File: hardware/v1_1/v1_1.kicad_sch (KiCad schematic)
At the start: 74 parts, among them J1 AUDIO IN, J2 MIDI OUT, J3 MIDI IN, J4 MIDI THRU, J5 OUTPUT R, J6 OUTPUT L - MONO, J7 EXP 2, J8 EXP 1, J9 Batt In, SW1 RotaryEncoder_Switch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

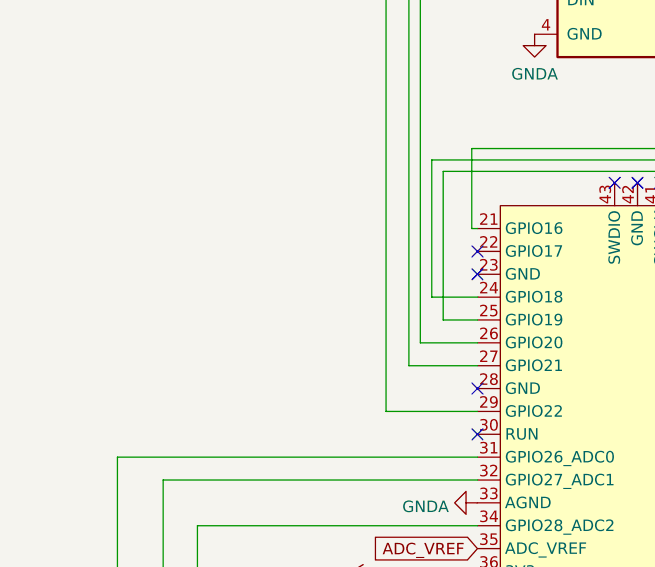
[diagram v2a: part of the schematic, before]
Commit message: Added low battery sensing on digitalPin
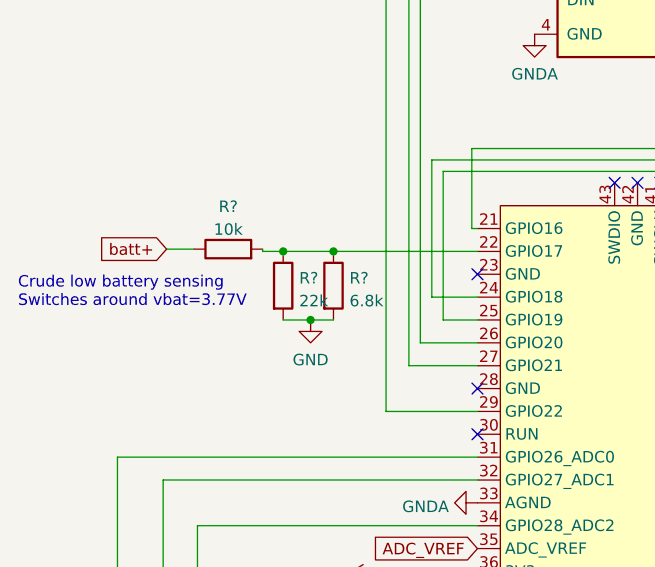
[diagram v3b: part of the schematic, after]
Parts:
- added R?: 10k, symbol Device:R
- added R?: 6.8k, symbol Device:R
- added R?: 22k, symbol Device:R
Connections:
- net GND: now also R?.2, R?.2
- net batt+: now also R?.1
- net at U2.22 (GPIO17): now also R?.1, R?.1, R?.2
- no-connect marks 47 -> 46
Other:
- note added: "Crude low battery sensing Switches around vbat=3.77V"
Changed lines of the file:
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@@
   (junction (at 156.845 100.33) (diameter 0) (color 0 0 0 0)
   )
+  (junction (at 47.498 77.47) (diameter 0) (color 0 0 0 0)
+  )
+  (junction (at 44.45 69.85) (diameter 0) (color 0 0 0 0)
+  )
   (junction (at 426.72 46.99) (diameter 0) (color 0 0 0 0)
   )
@@
   (junction (at 419.1 46.99) (diameter 0) (color 0 0 0 0)
   )
+  (junction (at 50.038 69.85) (diameter 0) (color 0 0 0 0)
+  )
   (junction (at 397.51 117.475) (diameter 0) (color 0 0 0 0)
   )
@@
   (no_connect (at 461.01 166.37))
   (no_connect (at 101.6 82.55))
-  (no_connect (at 66.04 69.85))
   (no_connect (at 468.63 82.55))
   (no_connect (at 67.945 132.08))
@@
     (stroke (width 0) (type default) (color 0 0 0 0))
   )
+  (wire (pts (xy 31.496 69.596) (xy 34.544 69.596))
+    (stroke (width 0) (type default) (color 0 0 0 0))
+  )
   (wire (pts (xy 92.71 179.705) (xy 92.71 185.42))
     (stroke (width 0) (type default) (color 0 0 0 0))
@@
     (stroke (width 0) (type default) (color 0 0 0 0))
   )
+  (wire (pts (xy 44.45 69.85) (xy 42.164 69.85))
+    (stroke (width 0) (type default) (color 0 0 0 0))
+  )
   (wire (pts (xy 163.195 15.24) (xy 163.195 19.05))
     (stroke (width 0) (type default) (color 0 0 0 0))
@@
     (stroke (width 0) (type default) (color 0 0 0 0))
   )
+  (wire (pts (xy 42.164 69.85) (xy 42.164 69.596))
+    (stroke (width 0) (type default) (color 0 0 0 0))
+  )
   (wire (pts (xy 439.42 113.538) (xy 441.96 113.538))
     (stroke (width 0) (type default) (color 0 0 0 0))
@@
     (stroke (width 0) (type default) (color 0 0 0 0))
   )
+  (wire (pts (xy 50.038 69.85) (xy 44.45 69.85))
+    (stroke (width 0) (type default) (color 0 0 0 0))
+  )
+  (wire (pts (xy 44.45 77.47) (xy 47.498 77.47))
+    (stroke (width 0) (type default) (color 0 0 0 0))
+  )
   (wire (pts (xy 450.85 59.69) (xy 457.835 59.69))
     (stroke (width 0) (type default) (color 0 0 0 0))
@@
     (stroke (width 0) (type default) (color 0 0 0 0))
   )
+  (wire (pts (xy 66.04 69.85) (xy 50.038 69.85))
+    (stroke (width 0) (type default) (color 0 0 0 0))
+  )
   (wire (pts (xy 149.225 78.74) (xy 149.225 67.31))
     (stroke (width 0) (type default) (color 0 0 0 0))
@@
     (stroke (width 0) (type default) (color 0 0 0 0))
   )
+  (wire (pts (xy 47.498 77.47) (xy 50.038 77.47))
+    (stroke (width 0) (type default) (color 0 0 0 0))
+  )
   (wire (pts (xy 130.81 30.48) (xy 136.525 30.48))
     (stroke (width 0) (type default) (color 0 0 0 0))
@@
     (effects (font (size 1.27 1.27)) (justify left bottom))
   )
+  (text "Crude low battery sensing\nSwitches around vbat=3.77V"
+    (at 14.986 76.2 0)
+    (effects (font (size 1.27 1.27)) (justify left bottom))
+  )
   (text "OR" (at 100.965 187.96 0)
     (effects (font (size 1.27 1.27)) (justify left bottom))
@@
     (effects (font (size 1.27 1.27)) (justify left bottom))
   )
+  (global_label "batt+" (shape input) (at 31.496 69.596 180) (fields_autoplaced)
+    (effects (font (size 1.27 1.27)) (justify right))
+    (property "Références Inter-Feuilles" "${INTERSHEET_REFS}" (id 0) (at 23.761 69.5166 0)
+      (effects (font (size 1.27 1.27)) (justify right) hide)
+    )
+  )
   (global_label "filtered_vcc" (shape input) (at 372.745 20.32 0) (fields_autoplaced)
     (effects (font (size 1.27 1.27)) (justify left))
@@
     (pin "1")
   )
+  (symbol (lib_id "Device:R") (at 38.354 69.596 90) (unit 1)
+    (in_bom yes) (on_board yes) (fields_autoplaced)
+    (property "Reference" "R?" (id 0) (at 38.354 64.8802 90))
+    (property "Value" "10k" (id 1) (at 38.354 67.4171 90))
+    (property "Footprint" "" (id 2) (at 38.354 71.374 90)
+      (effects (font (size 1.27 1.27)) hide)
+    )
+    (property "Datasheet" "~" (id 3) (at 38.354 69.596 0)
+      (effects (font (size 1.27 1.27)) hide)
+    )
+    (pin "1")
+    (pin "2")
+  )
   (symbol (lib_id "Amplifier_Operational:TL072") (at 85.09 177.8 0) (unit 2)
     (in_bom yes) (on_board yes) (fields_autoplaced)
@@
     (pin "1")
   )
+  (symbol (lib_id "power:GND") (at 47.498 77.47 0) (unit 1)
+    (in_bom yes) (on_board yes) (fields_autoplaced)
+    (property "Reference" "#PWR?" (id 0) (at 47.498 83.82 0)
+      (effects (font (size 1.27 1.27)) hide)
+    )
+    (property "Value" "GND" (id 1) (at 47.498 81.9134 0))
+    (property "Footprint" "" (id 2) (at 47.498 77.47 0)
+      (effects (font (size 1.27 1.27)) hide)
+    )
+    (property "Datasheet" "" (id 3) (at 47.498 77.47 0)
+      (effects (font (size 1.27 1.27)) hide)
+    )
+    (pin "1")
+  )
   (symbol (lib_id "Amplifier_Operational:TL074") (at 411.48 41.91 0) (unit 2)
     (in_bom yes) (on_board yes) (fields_autoplaced)
@@
     (pin "1")
   )
+  (symbol (lib_id "Device:R") (at 50.038 73.66 0) (unit 1)
+    (in_bom yes) (on_board yes) (fields_autoplaced)
+    (property "Reference" "R?" (id 0) (at 51.816 72.8253 0)
+      (effects (font (size 1.27 1.27)) (justify left))
+    )
+    (property "Value" "6.8k" (id 1) (at 51.816 75.3622 0)
+      (effects (font (size 1.27 1.27)) (justify left))
+    )
+    (property "Footprint" "" (id 2) (at 48.26 73.66 90)
+      (effects (font (size 1.27 1.27)) hide)
+    )
+    (property "Datasheet" "~" (id 3) (at 50.038 73.66 0)
+      (effects (font (size 1.27 1.27)) hide)
+    )
+    (pin "1")
+    (pin "2")
+  )
   (symbol (lib_id "Device:R") (at 274.955 125.095 0) (unit 1)
     (in_bom yes) (on_board yes) (fields_autoplaced)
@@
     (pin "1")
   )
+  (symbol (lib_id "Device:R") (at 44.45 73.66 0) (unit 1)
+    (in_bom yes) (on_board yes) (fields_autoplaced)
+    (property "Reference" "R?" (id 0) (at 46.228 72.8253 0)
+      (effects (font (size 1.27 1.27)) (justify left))
+    )
+    (property "Value" "22k" (id 1) (at 46.228 75.3622 0)
+      (effects (font (size 1.27 1.27)) (justify left))
+    )
+    (property "Footprint" "" (id 2) (at 42.672 73.66 90)
+      (effects (font (size 1.27 1.27)) hide)
+    )
+    (property "Datasheet" "~" (id 3) (at 44.45 73.66 0)
+      (effects (font (size 1.27 1.27)) hide)
+    )
+    (pin "1")
+    (pin "2")
+  )
   (symbol (lib_id "power:GNDA") (at 461.01 173.99 0) (unit 1)
     (in_bom yes) (on_board yes) (fields_autoplaced)
@@
       (reference "#PWR?") (unit 1) (value "+3V3") (footprint "")
     )
+    (path "/64073ef3-63c1-47ec-b4bf-1e1ce29231df"
+      (reference "#PWR?") (unit 1) (value "GND") (footprint "")
+    )
     (path "/6e25aba8-84dd-432e-bc26-a2faeb582ed8"
       (reference "#PWR?") (unit 1) (value "+3V3") (footprint "")
@@
       (reference "R20") (unit 1) (value "10") (footprint "Resistor_THT:R_Axial_DIN0207_L6.3mm_D2.5mm_P7.62mm_Horizontal")
     )
+    (path "/189038fc-9e70-431b-9406-9d4b69faa0ca"
+      (reference "R?") (unit 1) (value "10k") (footprint "")
+    )
+    (path "/c7b373c8-11dc-4503-9834-6bfd995fae71"
+      (reference "R?") (unit 1) (value "6.8k") (footprint "")
+    )
+    (path "/d4eff44b-f119-45e9-8040-631f11b7e450"
+      (reference "R?") (unit 1) (value "22k") (footprint "")
+    )
     (path "/1dbdedeb-a12d-4a03-88a7-8dc9f8b82f58"
